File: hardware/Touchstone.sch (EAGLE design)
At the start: 86 parts, among them J3 USB-MICROB, U1 NEOPIXEL_NANO_2427, U10 TSL2591, U11 915MHz, U12 MH-Z19, U13 CCS811-I2C, U14 IAQ-CORE-C, U15 VLP-450-F, U16 VLP-450-F, U17 LMV324QT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

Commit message: Updated BOM
Added MPN for all components
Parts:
- C11, C12, C15, C16, C17, C19, C20, C3, C5, C6, C7, C8: MPN (none) -> GRM155R71C104KA88J
- C18, C2, C23, C24: MPN (none) -> CC0402KRX5R6BB105
- C22, C9: MPN (none) -> GRJ155R60J106ME11D
- D1: MPN (none) -> SD103AW-13-F
- D3, D4: MPN (none) -> RB751S40T1G
- J3: MPN 47346-0001 -> ZX62-B-5PA(33)
- JP1: MPN (none) -> Helical antenna
- MK1: MPN (none) -> TOM-1545P-R
- R10, R13, R16, R21, R26, R28, R29, R30, R5, R6, R7: MPN (none) -> RC0402JR-0710KL
- R11, R15: MPN (none) -> RC0402JR-0727RL
- R12, R14, R9: MPN (none) -> RC0402FR-07100KL
- R17, R18, R4: MPN (none) -> RC0402JR-07470RL
- R19, R20, R22, R27: MPN (none) -> RC0402JR-071KL
- R23: MPN (none) -> RC0402FR-072K2L
- R24: MPN (none) -> RC0402JR-07470KL
- R25, R32: MPN (none) -> RC0402FR-07100RL
- R31: MPN (none) -> RC0402JR-0722KL
- S1: MPN (none) -> RS-032G05A3-SM RT
- U$4, U$5: MPN (none) -> 0878980426
- U$6: MPN (none) -> M50-3630442
- U1: MPN (none) -> 3484
- U11: MPN (none) -> RFM69HCW
- U13: MPN (none) -> CCS811
- U14: MPN (none) -> IAQ-CORE-C
- U15: MPN (none) -> VLP-650-F
- U16: MPN (none) -> VLP-550-F
- U17: MPN (none) -> LM324QT
- U2: MPN (none) -> FT231XQ-R
- U4: MPN (none) -> SI7021-A20-GM1
- U5: MPN (none) -> ATMEGA328P-MU
- U7: MPN (none) -> 20021311-00012T4LF
- U8: MPN MCP1703T-2502E/CB -> MCP1703T-3302E/CB
- X1: MPN (none) -> CSTCE16M0V53-R0

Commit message: Bug fixes
- Removed pullup from WAKE pin of CSS811 (stopped chip from working)
- Adjusted value of resistor on sound circuit to 1M (to increase gain to
a LOT)
- Minor trace and silkscreen adjustments
- BOM update
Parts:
- removed R14: 100K, Adafruit Feather 32u4 Bluefruit LE:MICROBUILDER_RESISTOR_0402MP
- R24: value 470K -> 1M; MPN RC0402JR-07470KL -> RC0402FR-071ML
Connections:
- net D5: no longer R14.2
- net VCC: no longer R14.1
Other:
- note added: "47K = low gain 100K = default gain 470K = high gain 1M = very high gain"
- note removed: "47K = low gain 100K = default gain 470K = high gain"
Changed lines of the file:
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@@
 <attribute name="MPN" value="RC0402FR-07100KL"/>
 </part>
-<part name="R14" library="Adafruit Feather 32u4 Bluefruit LE" deviceset="MICROBUILDER_RESISTOR" device="_0402MP" value="100K">
-<attribute name="MPN" value="RC0402FR-07100KL"/>
-</part>
 <part name="SUPPLY19" library="SparkFun-Aesthetics" deviceset="VCC" device=""/>
-<part name="SUPPLY20" library="SparkFun-Aesthetics" deviceset="VCC" device=""/>
 <part name="U$6" library="CONN_HDR_1.27MM_SMD_4POS" deviceset="CONN_HDR_1.27MM_SMD_4POS" device="">
 <attribute name="MPN" value="M50-3630442"/>
@@
 <attribute name="MPN" value="RC0402FR-072K2L"/>
 </part>
-<part name="R24" library="Adafruit PowerBoost 1000C Rev B" deviceset="MICROBUILDER_RESISTOR" device="_0402MP" value="470K">
-<attribute name="MPN" value="RC0402JR-07470KL"/>
+<part name="R24" library="Adafruit PowerBoost 1000C Rev B" deviceset="MICROBUILDER_RESISTOR" device="_0402MP" value="1M">
+<attribute name="MPN" value="RC0402FR-071ML"/>
 </part>
 <part name="SUPPLY22" library="SparkFun-PowerSymbols" deviceset="VCC" device=""/>
@@
 <text x="-10.16" y="66.04" size="1.27" layer="91" font="vector">47K = low gain
 100K = default gain
-470K = high gain</text>
+470K = high gain
+1M = very high gain</text>
 </plain>
 <instances>
@@
 <attribute name="MPN" x="121.92" y="20.32" size="1.778" layer="96" rot="R270" display="off"/>
 </instance>
-<instance part="R14" gate="G$1" x="172.72" y="20.32" rot="R270">
-<attribute name="MPN" x="172.72" y="20.32" size="1.778" layer="96" rot="R270" display="off"/>
-</instance>
 <instance part="SUPPLY19" gate="G$1" x="121.92" y="25.4"/>
-<instance part="SUPPLY20" gate="G$1" x="172.72" y="25.4"/>
 <instance part="U$6" gate="G$1" x="264.16" y="12.7">
 <attribute name="MPN" x="264.16" y="12.7" size="1.778" layer="96" display="off"/>
@@
 </segment>
 <segment>
-<pinref part="R14" gate="G$1" pin="1"/>
-<pinref part="SUPPLY20" gate="G$1" pin="VCC"/>
-</segment>
-<segment>
 <pinref part="U$6" gate="G$1" pin="P$1"/>
 <wire x1="274.32" y1="20.32" x2="276.86" y2="20.32" width="0.1524" layer="91"/>
@@
 <segment>
 <pinref part="U13" gate="G$1" pin="WAKE"/>
-<wire x1="165.1" y1="7.62" x2="170.18" y2="7.62" width="0.1524" layer="91"/>
+<wire x1="165.1" y1="7.62" x2="172.72" y2="7.62" width="0.1524" layer="91"/>
 <label x="165.1" y="7.62" size="1.778" layer="95"/>
-<wire x1="170.18" y1="7.62" x2="172.72" y2="7.62" width="0.1524" layer="91"/>
-<wire x1="170.18" y1="7.62" x2="170.18" y2="12.7" width="0.1524" layer="91"/>
-<junction x="170.18" y="7.62"/>
-<pinref part="R14" gate="G$1" pin="2"/>
-<wire x1="170.18" y1="12.7" x2="172.72" y2="12.7" width="0.1524" layer="91"/>
-<wire x1="172.72" y1="12.7" x2="172.72" y2="15.24" width="0.1524" layer="91"/>
-</segment>
-</net>
+</segment>
+</net>

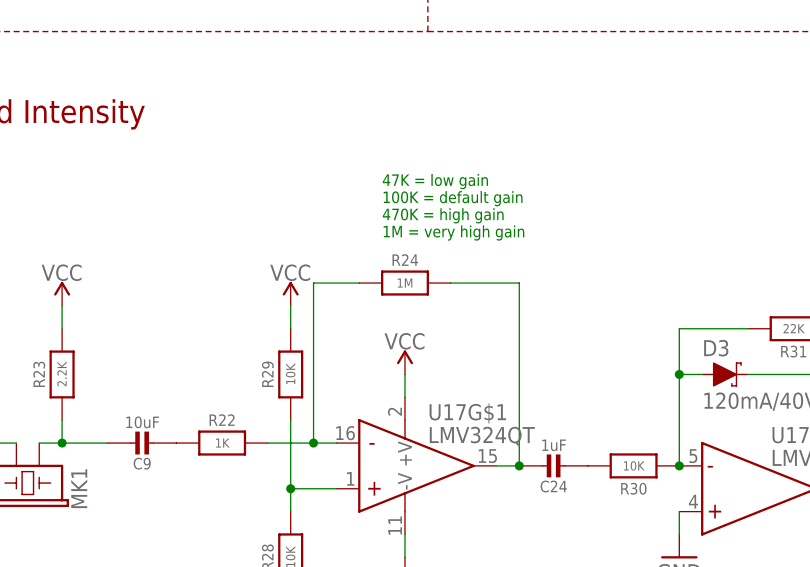
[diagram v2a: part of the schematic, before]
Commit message: Added gerbers and BOM
- Also updated firmware for button interrupt, sound level stuff
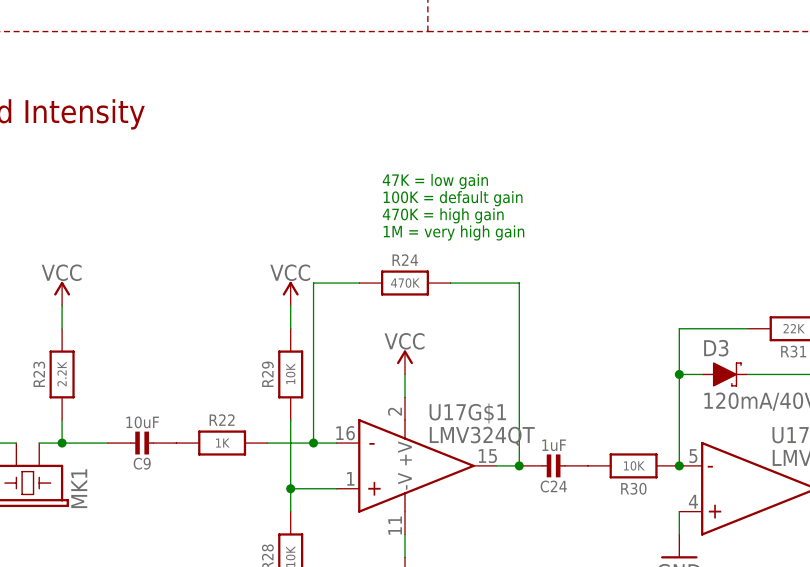
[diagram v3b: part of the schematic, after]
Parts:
- R24: value 1M -> 470K
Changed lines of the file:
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@@
 <attribute name="MPN" value="RC0402FR-072K2L"/>
 </part>
-<part name="R24" library="Adafruit PowerBoost 1000C Rev B" deviceset="MICROBUILDER_RESISTOR" device="_0402MP" value="1M">
+<part name="R24" library="Adafruit PowerBoost 1000C Rev B" deviceset="MICROBUILDER_RESISTOR" device="_0402MP" value="470K">
 <attribute name="MPN" value="RC0402FR-071ML"/>
 </part>
